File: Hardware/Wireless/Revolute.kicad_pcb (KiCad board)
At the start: 4 copper layers, 19.8 x 20 mm, 57 parts, among them U1 BQ27441-G1, U2 nrf52833_qfn40, U3 AS5600, U4 AP2112K-3.3, U5 BQ24075RGT, U6 Button, X1 32.768 kHz, X2 32MHZ

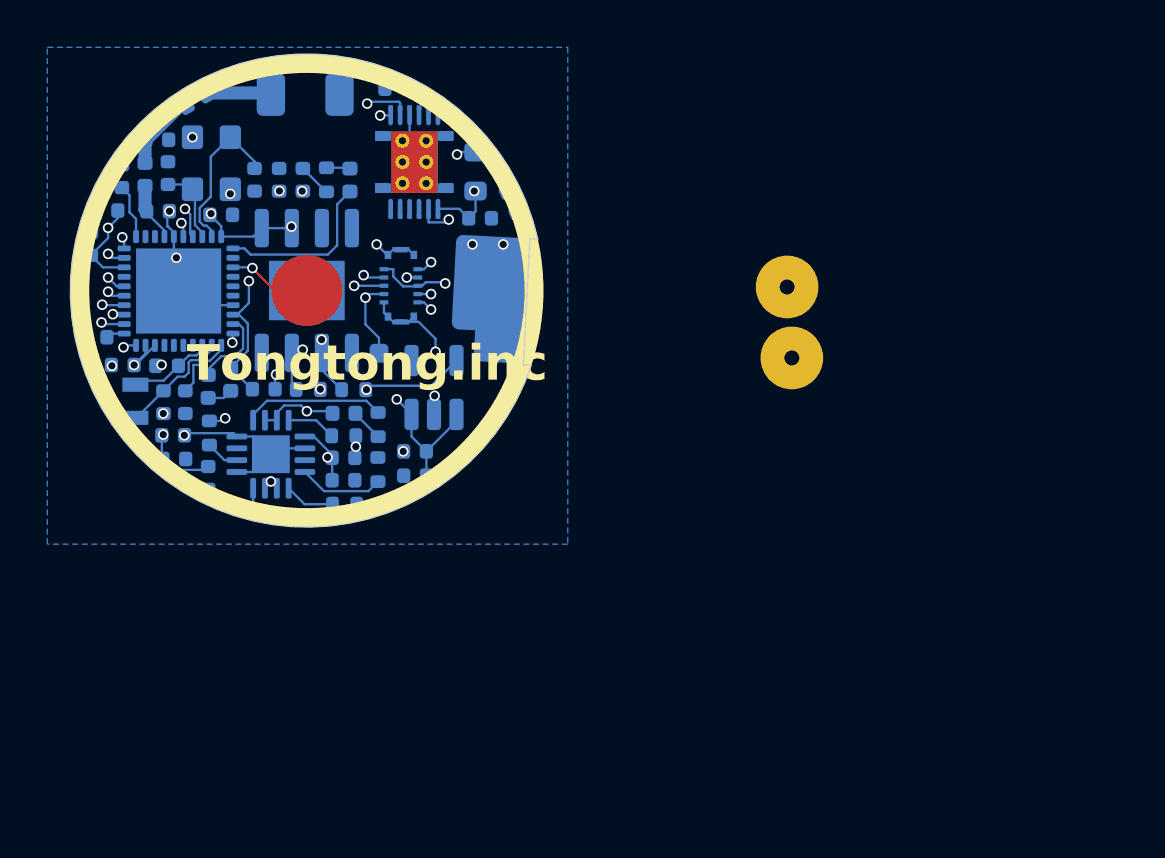
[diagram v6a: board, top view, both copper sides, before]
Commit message: added pogo charging pins, fixed debug connector
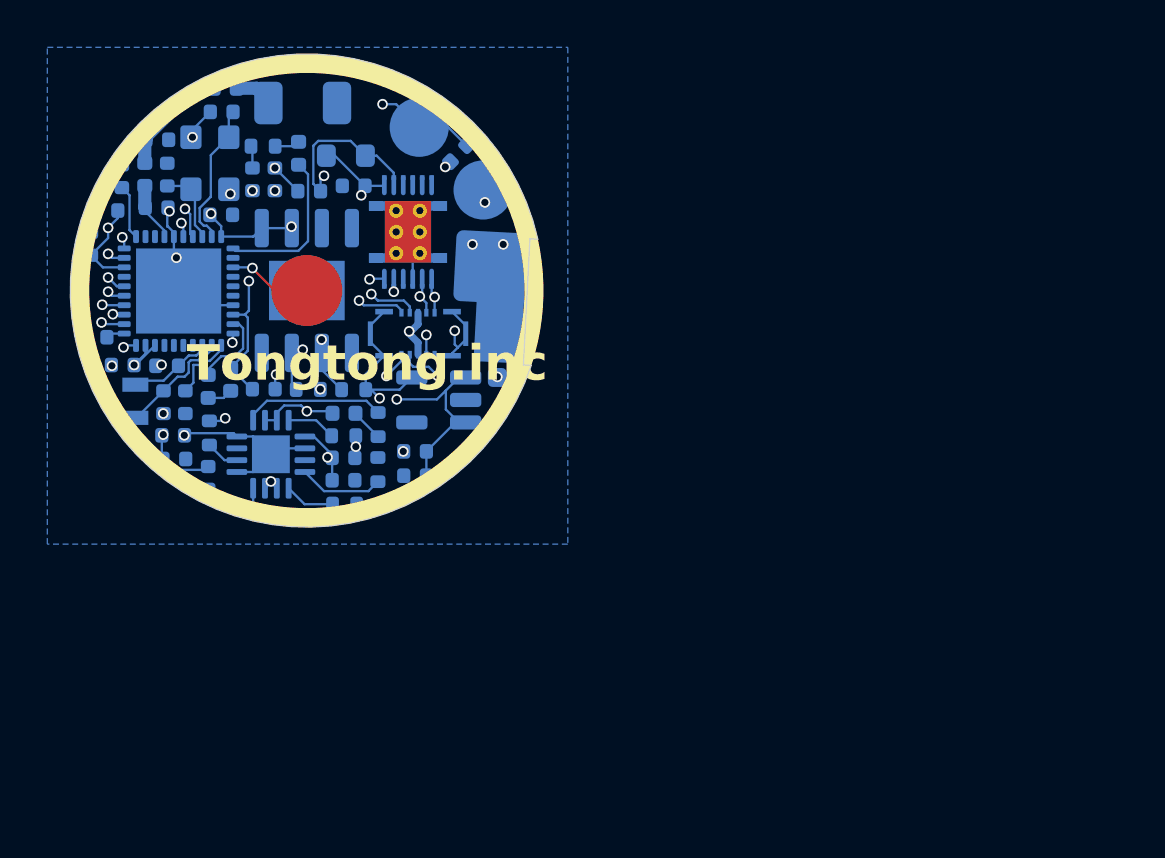
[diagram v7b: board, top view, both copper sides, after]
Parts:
- removed the ? at (191.3, 94.8)
- removed the REF** at (191.5, 97.8)
- removed U8: ~, Library:BK13C06-10DP
- added REF**: pogo_T1836, Library:pogo_T1836, B.Cu at (178.4, 90.8)
- added REF**: pogo_T1836, Library:pogo_T1836, B.Cu at (175.8, 88.1)
- added U7: ~, Library:BK13C06-10DS, B.Cu at (175.7, 96.8)
- moved C4 8.58 mm to (171.1, 90.8), turned to 180 degrees
- moved R1 5.52 mm to (172.7, 89.3), turned to 0 degrees
- moved C25 5.52 mm to (173.0, 90.6), turned to 0 degrees
- moved ? 5.10 mm to (179.1, 98.7)
- moved C12 3.80 mm to (177.4, 89.2), turned to 45 degrees
- moved C16 3.19 mm to (167.4, 87.5), turned to 0 degrees
- moved R2 3.03 mm to (169.2, 88.9), turned to 0 degrees
- moved U1 2.97 mm to (175.3, 92.5), turned to 90 degrees
- moved D1 2.45 mm to (170.7, 89.2)
- moved L4 1.33 mm to (167.6, 86.5), turned to 0 degrees
- moved C18 1.18 mm to (169.7, 90.3)
- moved C9 1.13 mm to (168.7, 90.3)
- moved ? 0.70 mm to (178.8, 94.0)
- moved U4 0.56 mm to (176.6, 99.6), turned to 180 degrees
- moved AE1 0.37 mm to (170.8, 87.1)
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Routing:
- net Batteryin: track 12.2 -> 23.4 mm
- net P0.15: track 31.5 -> 23.8 mm, vias 4 -> 3
- net VBUS: track 27.7 -> 34.5 mm, vias 3 -> 4
- net 1.8V: track 1.72 -> 8.23 mm, vias 0 -> 2
- net P0.17: track 27.1 -> 21.6 mm, vias 4 -> 3
- net GND: track 29.8 -> 34.9 mm, vias 26 -> 25
- net RESET: track 15.8 -> 20.3 mm, vias 2 -> 3
- net VDD_nRF: track 20.6 -> 24.0 mm, vias 9 -> 8
- net D-: track 16.8 -> 14.3 mm
- net OUT: track 17.6 -> 20.2 mm
- net Net-(C19-Pad2): track 3.29 -> 4.78 mm
- net Net-(U2-DEC4): track 16.5 -> 15.2 mm
- net swc: track 13.0 -> 14.3 mm
- net D+: track 19.4 -> 18.2 mm
- net Net-(U2-DEC3): track 7.04 -> 5.83 mm
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
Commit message: updated gerbers and bom
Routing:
- net OUT: track 20.2 -> 20.8 mm
- net VBUS: track 34.5 -> 35.1 mm
- net GND: vias 25 -> 26
